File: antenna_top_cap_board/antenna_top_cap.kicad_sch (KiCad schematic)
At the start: 53 parts, among them IC1 PCT2075DP,118, J1 Battery Charge Bypass, J10 BM04B-SRSS-TB(LF)(SN), J12 BM04B-SRSS-TB(LF)(SN), J14 BM04B-SRSS-TB(LF)(SN), J16 BM04B-SRSS-TB(LF)(SN), J2 Battery Charge Bypass, J3 Burn_Wire, J4 BM04B-SRSS-TB(LF)(SN), J6 Conn_Coaxial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

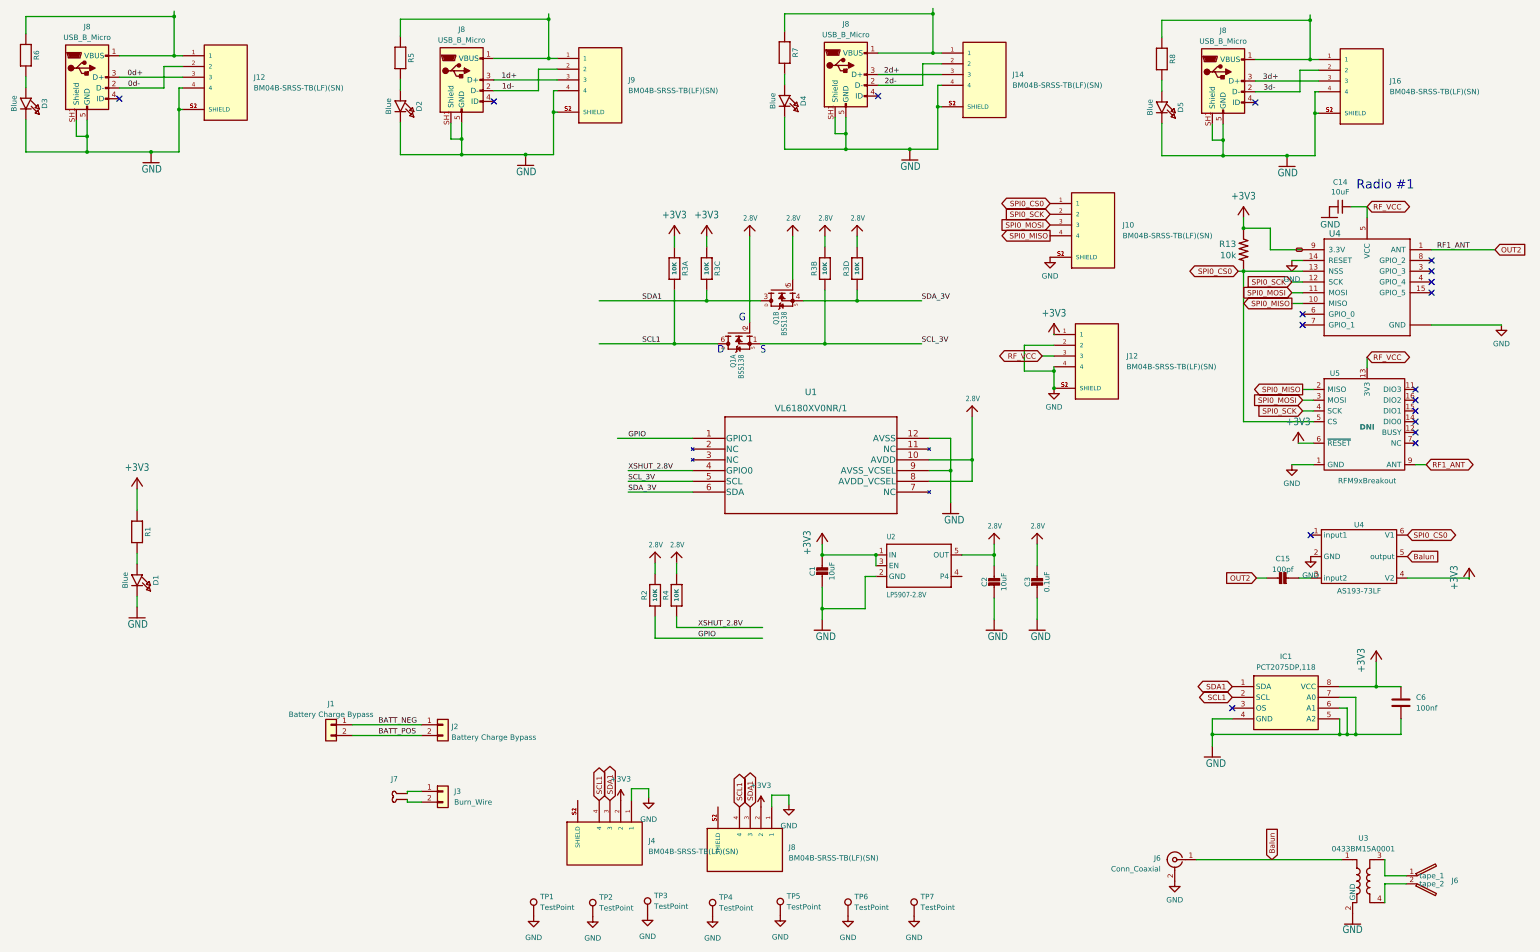
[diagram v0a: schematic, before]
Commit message: Started wiring with 12-pos connector for V3b
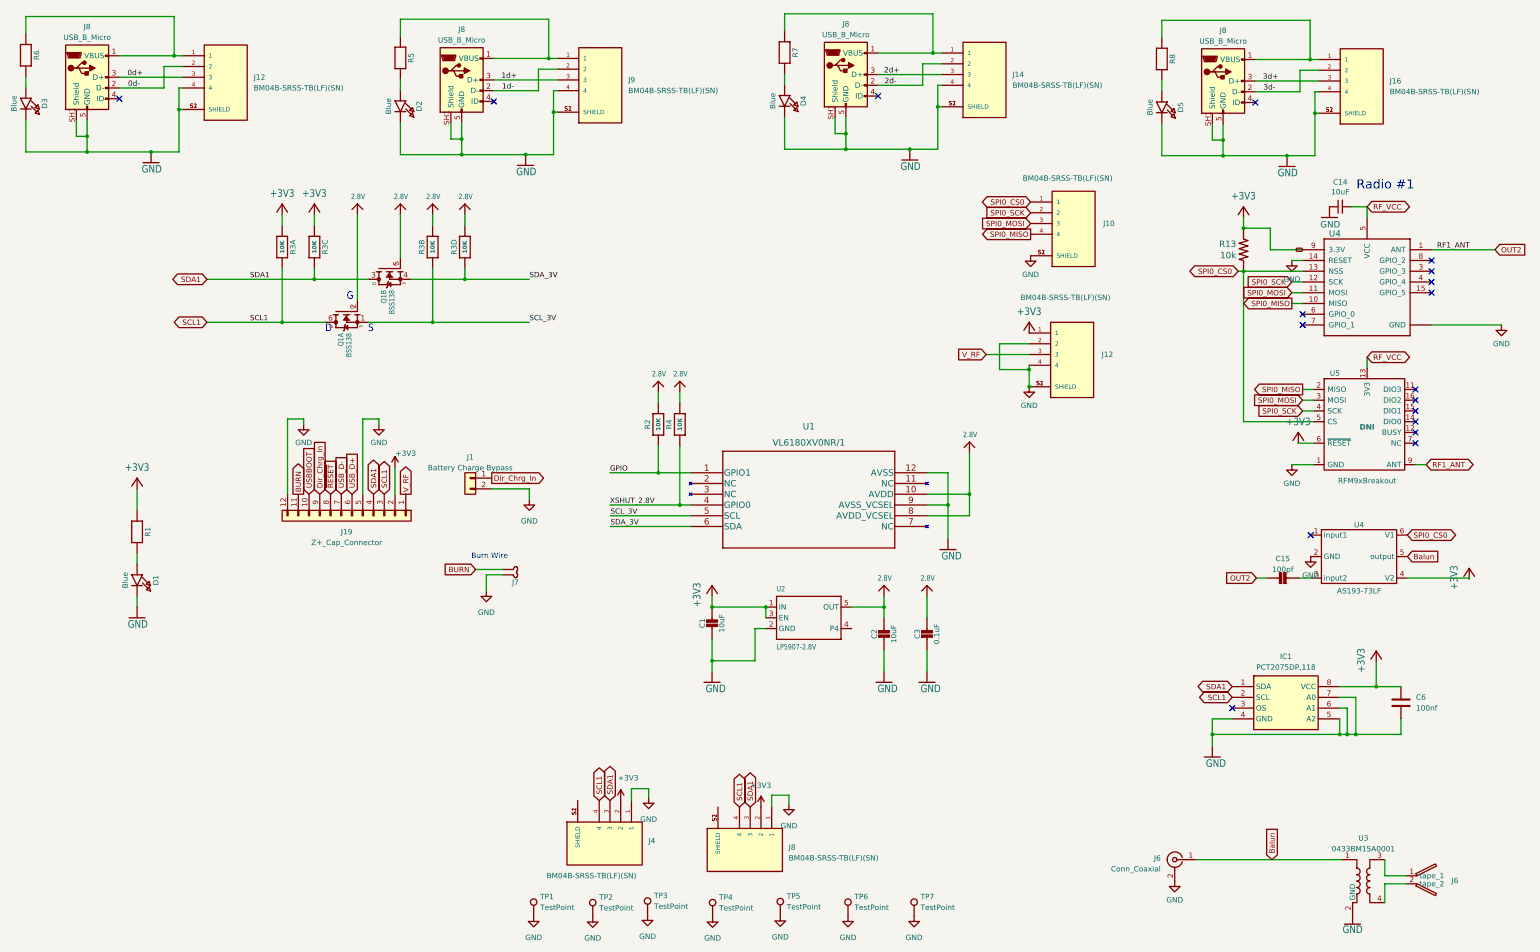
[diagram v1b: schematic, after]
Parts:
- removed J2: Battery Charge Bypass, Picolock2Pos:MOLEX_504050-0291, symbol Connector_Generic:Conn_01x02
- removed J3: Burn_Wire, Picolock2Pos:MOLEX_504050-0291, symbol Connector_Generic:Conn_01x02
- added J19: Z+_Cap_Connector, Connector_Molex:Molex_Pico-Lock_504050-1291_1x12-1MP_P1.50mm_Horizontal, symbol Connector_Generic:Conn_01x12
- U1: symbol VL6180X0NR:VL6180XV0NR/1 -> VL6180X0NR:VL6180XV0NR/1
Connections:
- net BATT_POS is gone; now on net GND: J1.2 (Pin_2)
- net +3V3: now also J19.2 (Pin_2)
- net GND: now also J7.1 (Power), J19.12 (Pin_12), J19.5 (Pin_5)
- net RF_VCC: no longer J12.3
- net SCL1: now also J19.3 (Pin_3)
- net SDA1: now also J19.4 (Pin_4)
- net BURN: now reaches J7.2 (GND)
- net BURN: now also J19.11 (Pin_11)
- net BATT_NEG renamed Dir_Chrg_In
- net Dir_Chrg_In: now also J19.9 (Pin_9)
- new net USBBOOT: J19.10 (Pin_10)
- new net USB_D+: J19.6 (Pin_6)
- new net USB_D-: J19.7 (Pin_7)
- new net V_RF: J12.3, J19.1 (Pin_1)
- new net ~{RESET}: J19.8 (Pin_8)
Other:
- note added: "Burn Wire"
- moved on the sheet: C1, C2, C3, J1, J10, J12, J7, Q1A, Q1B, R3A, R3B, R3C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

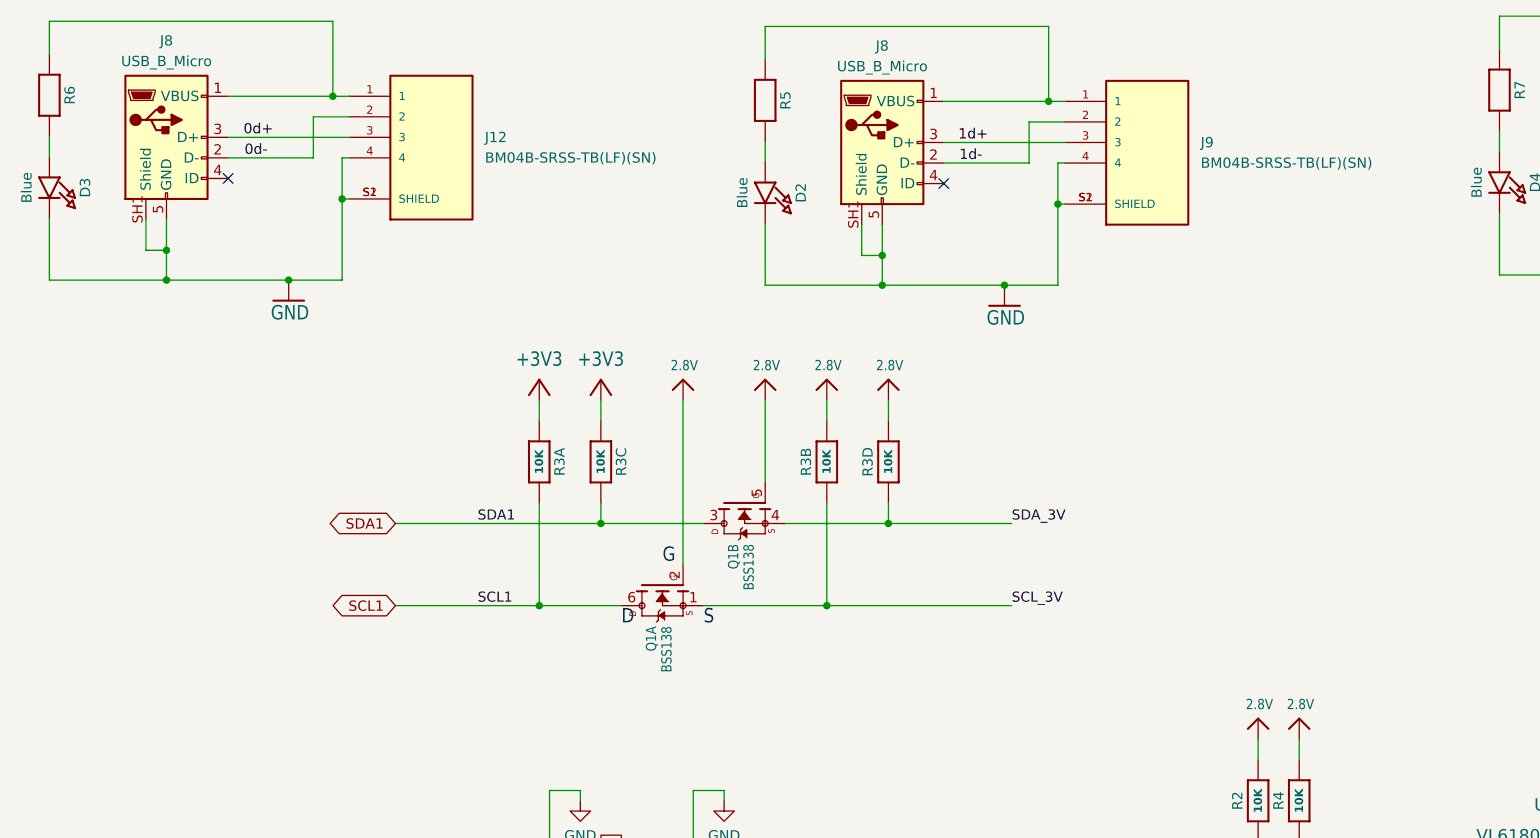
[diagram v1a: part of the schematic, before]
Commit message: Connected USB Breakout
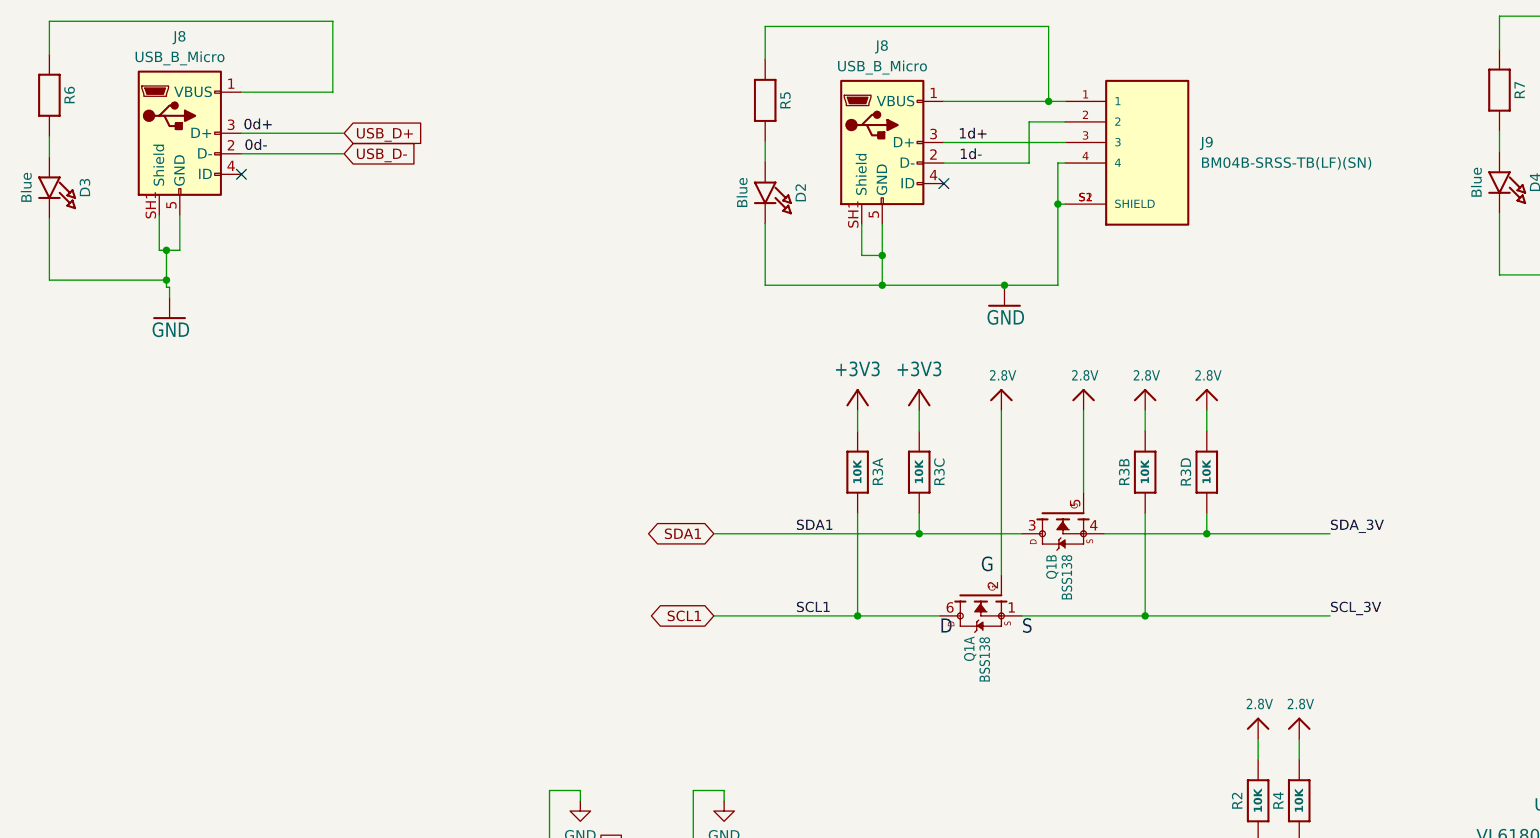
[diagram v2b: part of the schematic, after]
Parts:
- removed J12: BM04B-SRSS-TB(LF)(SN), Antenna_board:JST_BM04B-SRSS-TB(LF)(SN), symbol BM04B-SRSS-TB_LF__SN_:BM04B-SRSS-TB(LF)(SN)
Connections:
- net 0d+ is gone; now on net USB_D+: J8.3 (D+)
- net 0d- is gone; now on net USB_D-: J8.2 (D-)
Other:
- moved on the sheet: J8, Q1A, Q1B, R3A, R3B, R3C, R3D

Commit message: Finished Connecting 12Pos Connections
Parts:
- added J2, J3: Conn_01x02, Connector_PinHeader_2.54mm:PinHeader_1x02_P2.54mm_Vertical, symbol Connector_Generic:Conn_01x02
- added JP1: SolderJumper_3_Open, Jumper:SolderJumper-3_P1.3mm_Open_RoundedPad1.0x1.5mm_NumberLabels, symbol Jumper:SolderJumper_3_Open
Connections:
- net +3V3: now also JP1.1 (A)
- net GND: now also J2.2 (Pin_2), J3.2 (Pin_2)
- net RF_VCC: now also JP1.2 (C)
- net USBBOOT: now also J2.1 (Pin_1)
- net V_RF: now also JP1.3 (B)
- net ~{RESET}: now also J3.1 (Pin_1)
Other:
- moved on the sheet: J1, J19

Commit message: Addressed all DRC Errors
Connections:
- no-connect marks 18 -> 20
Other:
- moved on the sheet: J8
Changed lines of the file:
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@@
 	)
 	(no_connect
+		(at 187.96 212.09)
+	)
+	(no_connect
 		(at 359.283 88.265)
 	)
@@
 	)
 	(no_connect
+		(at 157.48 210.82)
+	)
+	(no_connect
 		(at 312.166 188.976)
 	)
@@
 	(wire
 		(pts
-			(xy 203.327 212.344) (xy 203.327 209.55)
+			(xy 200.66 212.09) (xy 200.66 209.296)
 		)
 		(stroke
@@
 	(wire
 		(pts
-			(xy 203.327 209.55) (xy 207.391 209.55)
+			(xy 200.66 209.296) (xy 204.724 209.296)
 		)
 		(stroke
@@
 	(wire
 		(pts
-			(xy 207.391 209.55) (xy 207.391 211.709)
+			(xy 204.724 209.296) (xy 204.724 211.455)
 		)
 		(stroke
@@
 	(global_label "SDA1"
 		(shape bidirectional)
-		(at 198.247 212.344 90)
+		(at 195.58 212.09 90)
 		(fields_autoplaced yes)
 		(effects
@@
 		)
 		(property "Intersheetrefs" "${INTERSHEET_REFS}"
-			(at 198.247 203.5493 90)
+			(at 195.58 203.2953 90)
 			(effects
 				(font
@@
 	(global_label "SCL1"
 		(shape bidirectional)
-		(at 195.707 212.344 90)
+		(at 193.04 212.09 90)
 		(fields_autoplaced yes)
 		(effects
@@
 		)
 		(property "Intersheetrefs" "${INTERSHEET_REFS}"
-			(at 195.707 203.6098 90)
+			(at 193.04 203.3558 90)
 			(effects
 				(font
@@
 	(symbol
 		(lib_id "power:+3V3")
-		(at 200.787 212.344 0)
+		(at 198.12 212.09 0)
 		(unit 1)
 		(exclude_from_sim no)
@@
 		(fields_autoplaced yes)
 		(property "Reference" "#PWR053"
-			(at 200.787 216.154 0)
+			(at 198.12 215.9 0)
 			(effects
 				(font
@@
 		)
 		(property "Value" "+3V3"
-			(at 200.787 207.264 0)
+			(at 198.12 207.01 0)
 			(effects
 				(font
@@
 		)
 		(property "Footprint" ""
-			(at 200.787 212.344 0)
+			(at 198.12 212.09 0)
 			(effects
 				(font
@@
 		)
 		(property "Datasheet" ""
-			(at 200.787 212.344 0)
+			(at 198.12 212.09 0)
 			(effects
 				(font
@@
 		)
 		(property "Description" ""
-			(at 200.787 212.344 0)
+			(at 198.12 212.09 0)
 			(effects
 				(font
@@
 	(symbol
 		(lib_id "BM04B-SRSS-TB_LF__SN_:BM04B-SRSS-TB(LF)(SN)")
-		(at 195.707 222.504 270)
+		(at 193.04 222.25 270)
 		(unit 1)
 		(exclude_from_sim no)
@@
 		(fields_autoplaced yes)
 		(property "Reference" "J8"
-			(at 207.3402 221.869 90)
+			(at 204.6732 221.615 90)
 			(effects
 				(font
@@
 		)
 		(property "Value" "BM04B-SRSS-TB(LF)(SN)"
-			(at 207.3402 224.409 90)
+			(at 204.6732 224.155 90)
 			(effects
 				(font
@@
 		)
 		(property "Footprint" "Antenna_board:JST_BM04B-SRSS-TB(LF)(SN)"
-			(at 195.707 222.504 0)
+			(at 193.04 222.25 0)
 			(effects
 				(font
@@
 		)
 		(property "Datasheet" ""
-			(at 195.707 222.504 0)
+			(at 193.04 222.25 0)
 			(effects
 				(font
@@
 		)
 		(property "Description" ""
-			(at 195.707 222.504 0)
+			(at 193.04 222.25 0)
 			(effects
 				(font
@@
 		)
 		(property "PARTREV" "N/A"
-			(at 195.707 222.504 0)
+			(at 193.04 222.25 0)
 			(effects
 				(font
@@
 		)
 		(property "SNAPEDA_PN" "BM04B-SRSS-TB(LF)(SN)"
-			(at 195.707 222.504 0)
+			(at 193.04 222.25 0)
 			(effects
 				(font
@@
 		)
 		(property "STANDARD" "Manufacturer Recommendations"
-			(at 195.707 222.504 0)
+			(at 193.04 222.25 0)
 			(effects
 				(font
@@
 		)
 		(property "MAXIMUM_PACKAGE_HEIGHT" "6.3 mm"
-			(at 195.707 222.504 0)
+			(at 193.04 222.25 0)
 			(effects
 				(font
@@
 		)
 		(property "MANUFACTURER" "JST Sales America Inc."
-			(at 195.707 222.504 0)
+			(at 193.04 222.25 0)
 			(effects
 				(font
@@
 	(symbol
 		(lib_id "power:GND")
-		(at 207.391 211.709 0)
+		(at 204.724 211.455 0)
 		(unit 1)
 		(exclude_from_sim no)
@@
 		(fields_autoplaced yes)
 		(property "Reference" "#PWR054"
-			(at 207.391 218.059 0)
+			(at 204.724 217.805 0)
 			(effects
 				(font
@@
 		)
 		(property "Value" "GND"
-			(at 207.391 216.789 0)
+			(at 204.724 216.535 0)
 			(effects
 				(font
@@
 		)
 		(property "Footprint" ""
-			(at 207.391 211.709 0)
+			(at 204.724 211.455 0)
 			(effects
 				(font
@@
 		)
 		(property "Datasheet" ""
-			(at 207.391 211.709 0)
+			(at 204.724 211.455 0)
 			(effects
 				(font
@@
 		)
 		(property "Description" ""
-			(at 207.391 211.709 0)
+			(at 204.724 211.455 0)
 			(effects
 				(font

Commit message: Added Jumper to Aux RF Line
Added an 0603 Jumper to break the Aux RF connection when not in use
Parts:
- added R10: DNI, Resistor_SMD:R_0603_1608Metric, symbol Device:R_US
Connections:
- net Balun: now also R10.1; no longer J6.1 (In), U3.1
- new net: J6.1 (In), R10.2, U3.1
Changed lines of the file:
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@@
 	)
 	(junction
+		(at 322.58 224.79)
+		(diameter 0)
+		(color 0 0 0 0)
+	)
+	(junction
 		(at 264.16 108.966)
 		(diameter 0)
@@
 	(wire
 		(pts
+			(xy 322.58 224.79) (xy 338.074 224.79)
+		)
+		(stroke
+			(width 0)
+			(type default)
+		)
+	)
+	(wire
+		(pts
 			(xy 41.91 59.69) (xy 41.91 58.42)
 		)
@@
 	(wire
 		(pts
-			(xy 303.657 224.79) (xy 338.074 224.79)
+			(xy 303.657 224.79) (xy 322.58 224.79)
 		)
 		(stroke
@@
 	(wire
 		(pts
+			(xy 322.58 213.36) (xy 322.58 215.9)
+		)
+		(stroke
+			(width 0)
+			(type default)
+		)
+	)
+	(wire
+		(pts
 			(xy 137.668 40.513) (xy 152.654 40.513)
 		)
@@
 	(wire
 		(pts
+			(xy 322.58 223.52) (xy 322.58 224.79)
+		)
+		(stroke
+			(width 0)
+			(type default)
+		)
+	)
+	(wire
+		(pts
 			(xy 242.57 41.783) (xy 242.57 46.863)
 		)
@@
 	(global_label "Balun"
 		(shape input)
-		(at 321.564 224.79 90)
+		(at 322.58 213.36 90)
 		(fields_autoplaced yes)
 		(effects
@@
 		)
 		(property "Intersheetrefs" "${INTERSHEET_REFS}"
-			(at 321.564 216.502 90)
+			(at 322.58 205.072 90)
 			(effects
 				(font
@@
 					(unit 1)
 				)
+			)
+		)
+	)
+	(symbol
+		(lib_id "Device:R_US")
+		(at 322.58 219.71 0)
+		(unit 1)
+		(exclude_from_sim no)
+		(in_bom yes)
+		(on_board yes)
+		(dnp no)
+		(fields_autoplaced yes)
+		(property "Reference" "R10"
+			(at 325.12 218.4399 0)
+			(effects
+				(font
+					(size 1.27 1.27)
+				)
+				(justify left)
+			)
+		)
+		(property "Value" "DNI"
+			(at 325.12 220.9799 0)
+			(effects
+				(font
+					(size 1.27 1.27)
+				)
+				(justify left)
+			)
+		)
+		(property "Footprint" "Resistor_SMD:R_0603_1608Metric"
+			(at 323.596 219.964 90)
+			(effects
+				(font
+					(size 1.27 1.27)
+				)
+				(hide yes)
+			)
+		)
+		(property "Datasheet" "~"
+			(at 322.58 219.71 0)
+			(effects
+				(font
+					(size 1.27 1.27)
+				)
+				(hide yes)
+			)
+		)
+		(property "Description" "Resistor, US symbol"
+			(at 322.58 219.71 0)
+			(effects
+				(font
+					(size 1.27 1.27)
+				)
+				(hide yes)
+			)
+		)
+		(pin "2"
+		)
+		(pin "1"
+		)
+		(instances
+			(project "antenna_top_cap"
+				(path "/e63e39d7-6ac0-4ffd-8aa3-1841a4541b55"
+					(reference "R10")
+					(unit 1)
+				)
